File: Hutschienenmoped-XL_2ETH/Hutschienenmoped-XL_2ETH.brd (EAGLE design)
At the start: 166.3 x 101.8 mm, 129 parts, among them J1 638207222005, J13 638207222005, J15 638207222008, J2 645004114822, J4 61300421121, J7 638207222005, J8 638207222007, U4 TLE9250VSJ

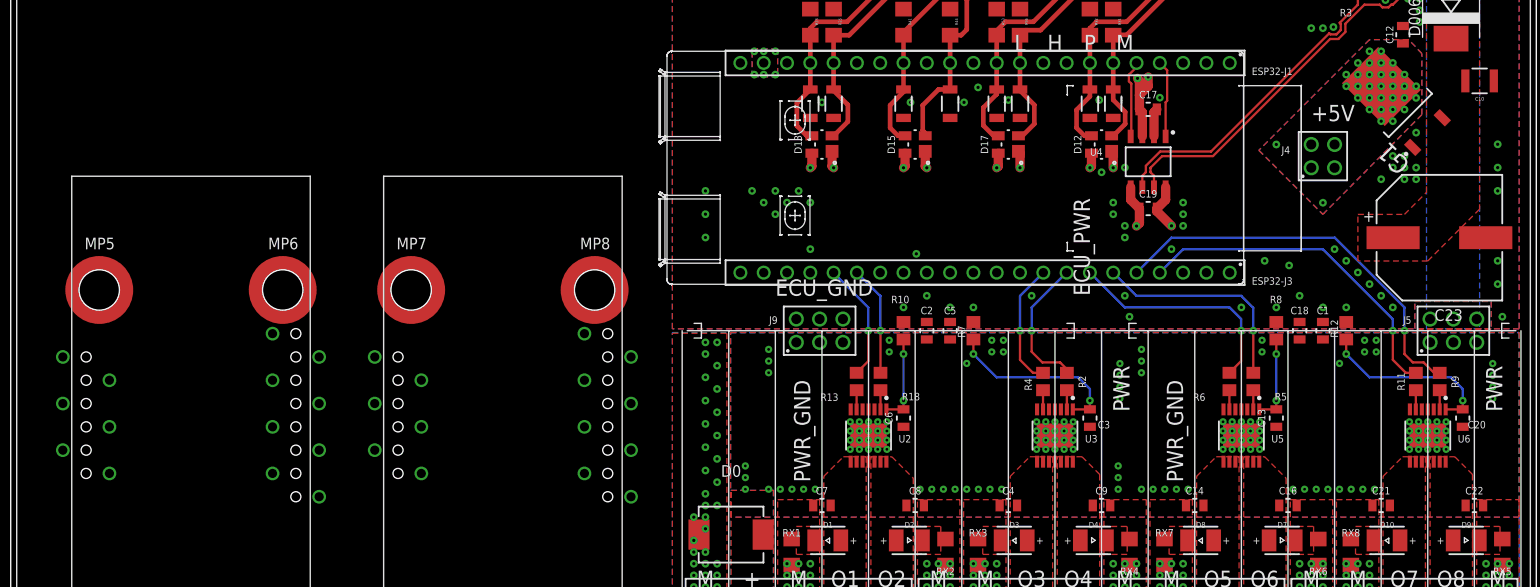
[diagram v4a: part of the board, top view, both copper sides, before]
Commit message: Update grid settings, change font display, adjust pad sizes and hole drills, add new package with 10-pin socket header, modify parameter values for pads and vias. Add symbol for 10-pin socket header THT.
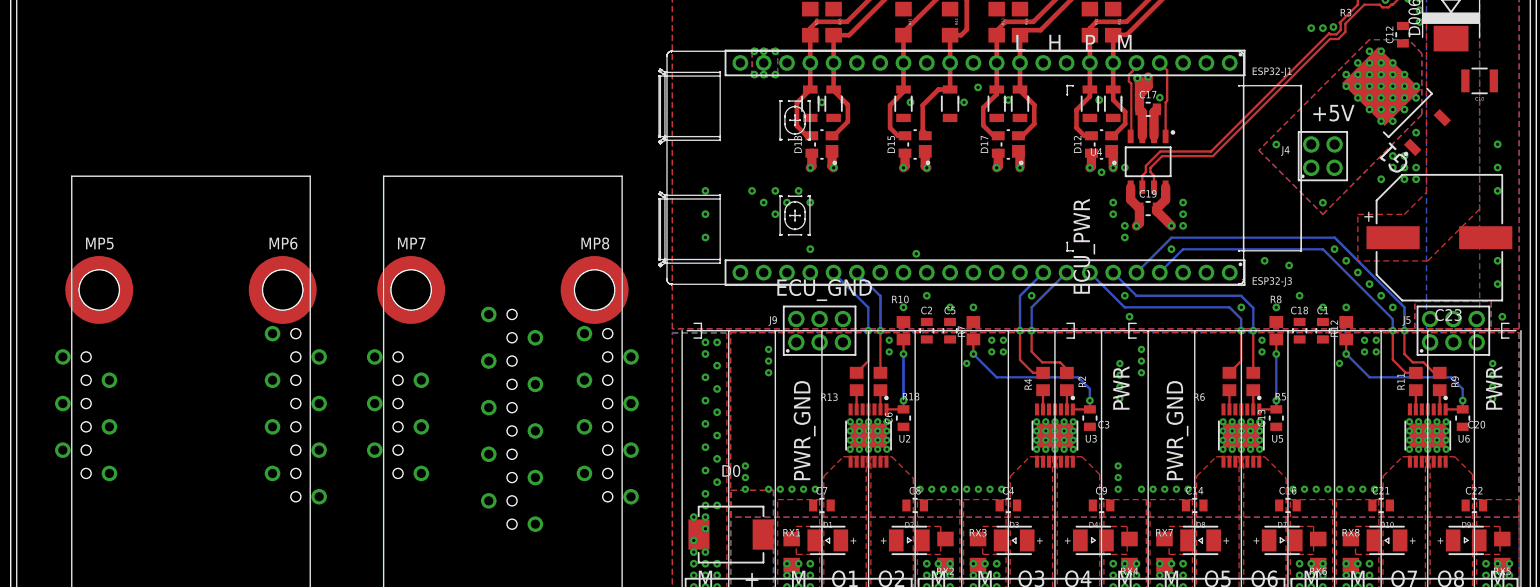
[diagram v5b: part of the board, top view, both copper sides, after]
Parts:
- added J3: 61301015721, Wurth_Connectors_WR-PHD:61301015721
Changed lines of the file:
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@@
 <drawing>
 <settings>
-<setting alwaysvectorfont="no"/>
+<setting alwaysvectorfont="yes"/>
 <setting verticaltext="up"/>
 </settings>
-<grid distance="32.4" unitdist="mm" unit="mm" style="lines" multiple="1" display="yes" altdistance="5" altunitdist="mil" altunit="mil"/>
+<grid distance="1" unitdist="mm" unit="mm" style="lines" multiple="1" display="yes" altdistance="5" altunitdist="mil" altunit="mil"/>
 <layers>
 <layer number="1" name="Top" color="4" fill="1" visible="yes" active="yes"/>
@@
 </layers>
 <board>
-<fusionsync huburn="a.YnVzaW5lc3M6bXNtdWM" projecturn="a.YnVzaW5lc3M6bXNtdWMjMjAyMjAzMTc1MDgxMzE4ODE" f3durn="urn:adsk.wipprod:dm.lineage:ajjTPt2gRBKkWSmyFLQsrw" pcbguid="b123e0b9-a0e3-403d-924e-517ce26273dc" lastpulledtime="2023-10-23T01:33:52Z" lastsyncedchangeguid="" latestrevisionid="f66c36f4-6c79-41b0-bf2f-e42f6f080a47" lastsyncedrevisionid="f66c36f4-6c79-41b0-bf2f-e42f6f080a47" lastboardhashguid="1047857f-715c-b88c-f26d-1f0562ae35e4" lastpushedtime="2024-03-24T11:42:32Z" linktopcb3d="true"/>
+<fusionsync huburn="a.YnVzaW5lc3M6bXNtdWM" projecturn="a.YnVzaW5lc3M6bXNtdWMjMjAyMjAzMTc1MDgxMzE4ODE" f3durn="urn:adsk.wipprod:dm.lineage:ajjTPt2gRBKkWSmyFLQsrw" pcbguid="" lastpulledtime="2023-10-23T01:33:52Z" lastsyncedchangeguid="" latestrevisionid="4beeb25c-c3ea-4695-891d-5bfc398b937a" lastsyncedrevisionid="4beeb25c-c3ea-4695-891d-5bfc398b937a" lastboardhashguid="d47e81b0-323d-8e0b-e760-b965a1c6aebf" lastpushedtime="2024-03-24T11:47:00Z" linktopcb3d="true"/>
 <plain>
 <wire x1="52.04" y1="41.46" x2="50.54" y2="41.46" width="0.1524" layer="22"/>
@@
 <param name="rvMicroViaOuter" value="0"/>
 <param name="rvMicroViaInner" value="0"/>
-<param name="rlMinPadTop" value="0.25mm"/>
+<param name="rlMinPadTop" value="0.35mm"/>
 <param name="rlMaxPadTop" value="0.5mm"/>
 <param name="rlMinPadInner" value="0.15mm"/>
 <param name="rlMaxPadInner" value="0.3mm"/>
-<param name="rlMinPadBottom" value="0.25mm"/>
+<param name="rlMinPadBottom" value="0.35mm"/>
 <param name="rlMaxPadBottom" value="0.5mm"/>
 <param name="rlMinViaOuter" value="0.25mm"/>
@@
 <attribute name="VALUE" x="-7.4622" y="20.1228" size="1.016" layer="28" rot="MR90" align="bottom-right"/>
 </element>
+<element name="J3" library="Wurth_Connectors_WR-PHD" library_urn="urn:adsk.eagle:library:14804658" package="61301015721" package3d_urn="urn:adsk.eagle:package:14805620/2" value=" 61301015721 " x="-16" y="31" smashed="yes" rot="MR270">
+<attribute name="DATASHEET-URL" value="https://www.we-online.com/redexpert/spec/61301015721?ae" x="-16" y="31" size="1.778" layer="28" rot="MR270" display="off"/>
+<attribute name="GENDER" value="Socket Header" x="-16" y="31" size="1.778" layer="28" rot="MR270" display="off"/>
+<attribute name="IR" value="3A" x="-16" y="31" size="1.778" layer="28" rot="MR270" display="off"/>
+<attribute name="MOUNT" value="THT" x="-16" y="31" size="1.778" layer="28" rot="MR270" display="off"/>
+<attribute name="NAME" x="-16.7541" y="44.9272" size="1.016" layer="26" rot="MR270" align="bottom-right"/>
+<attribute name="PACKAGING" value="Tube" x="-16" y="31" size="1.778" layer="28" rot="MR270" display="off"/>
+<attribute name="PART-NUMBER" value=" 61301015721 " x="-16" y="31" size="1.778" layer="28" rot="MR270" display="off"/>
+<attribute name="PINS" value=" 10 " x="-16" y="31" size="1.778" layer="28" rot="MR270" display="off"/>
+<attribute name="PITCH" value="2.54mm" x="-16" y="31" size="1.778" layer="28" rot="MR270" display="off"/>
+<attribute name="ROWS" value="Single" x="-16" y="31" size="1.778" layer="28" rot="MR270" display="off"/>
+<attribute name="TYPE" value="Bottom Entry" x="-16" y="31" size="1.778" layer="28" rot="MR270" display="off"/>
+<attribute name="VALUE" x="-14.1078" y="44.8672" size="1.016" layer="28" rot="MR270" align="bottom-right"/>
+</element>
 </elements>

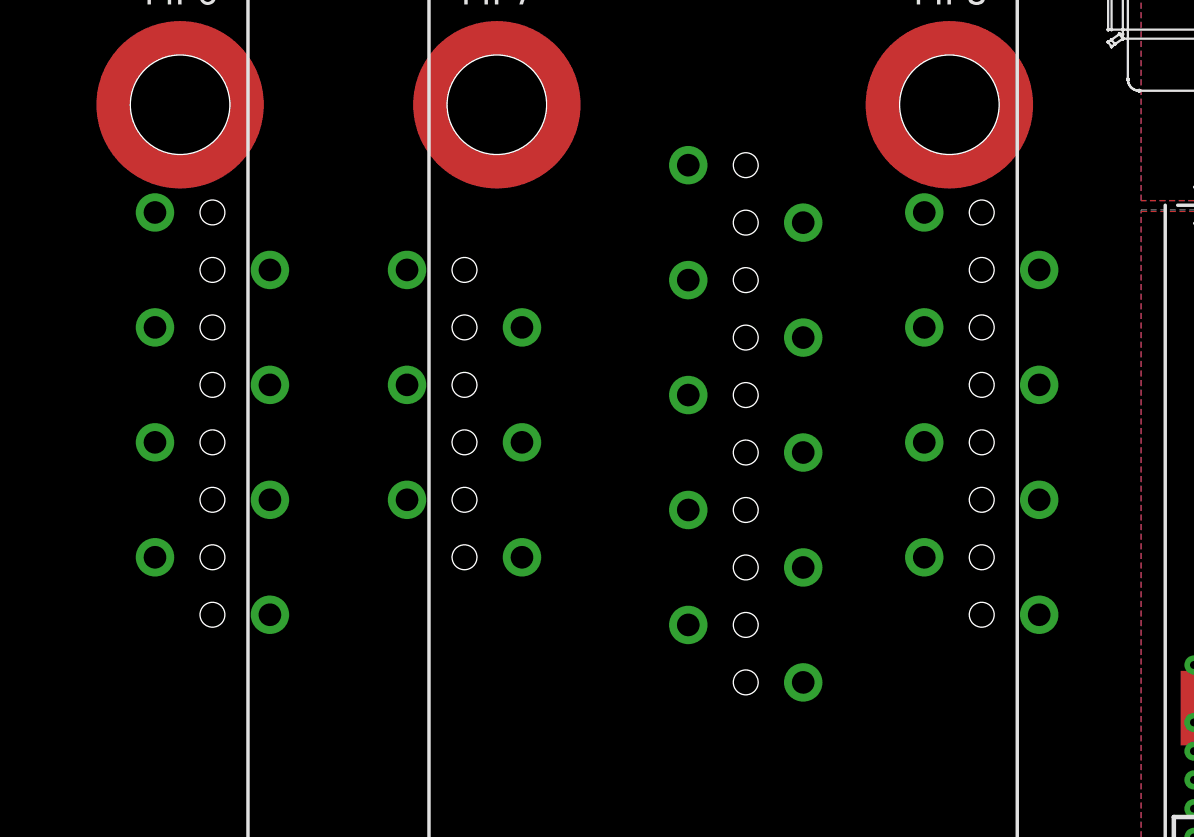
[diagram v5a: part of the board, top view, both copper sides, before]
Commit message: Update layer visibility settings for various elements.
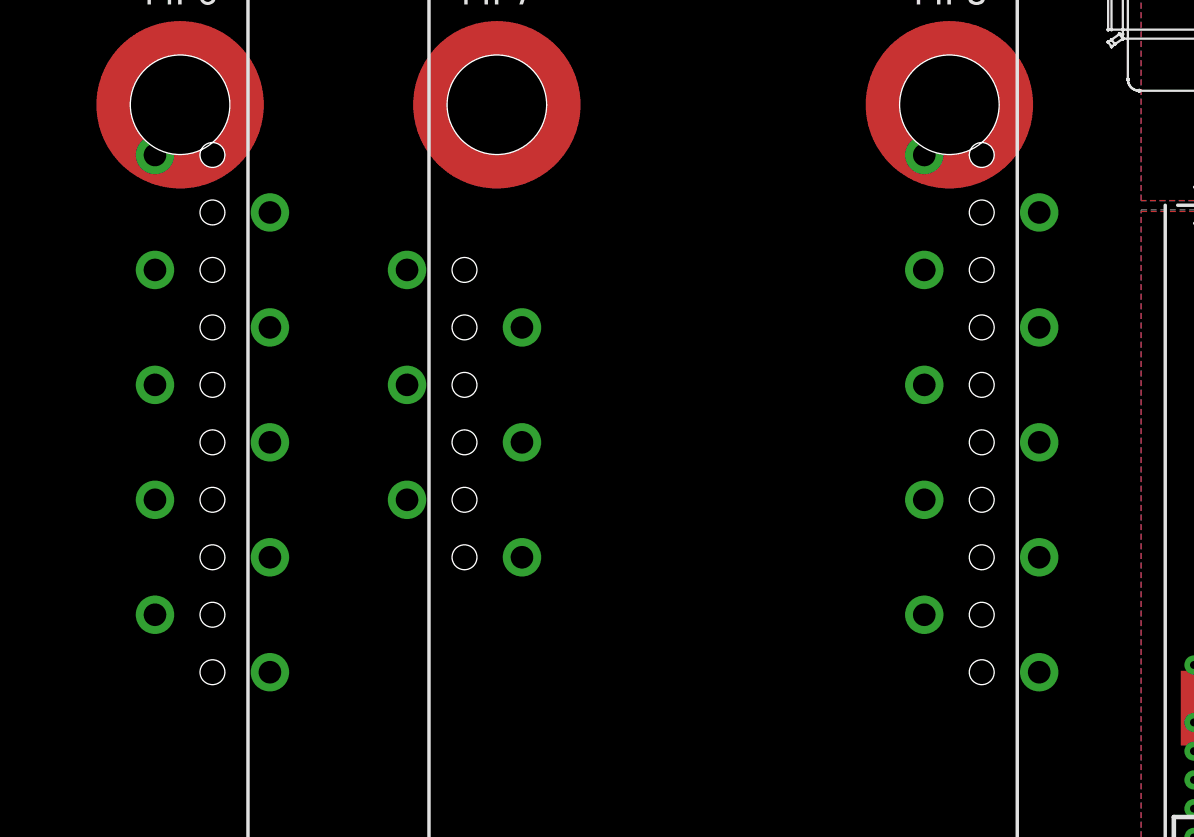
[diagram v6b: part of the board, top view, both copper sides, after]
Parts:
- removed J3: 61301015721, Wurth_Connectors_WR-PHD:61301015721
- W1-J1, W2-J1: value 61300815721 -> 61301015721; device Wurth_Connectors_WR-PHD:61300815721 -> WE-special:61301015721
- turned W1-J1 to 90 degrees

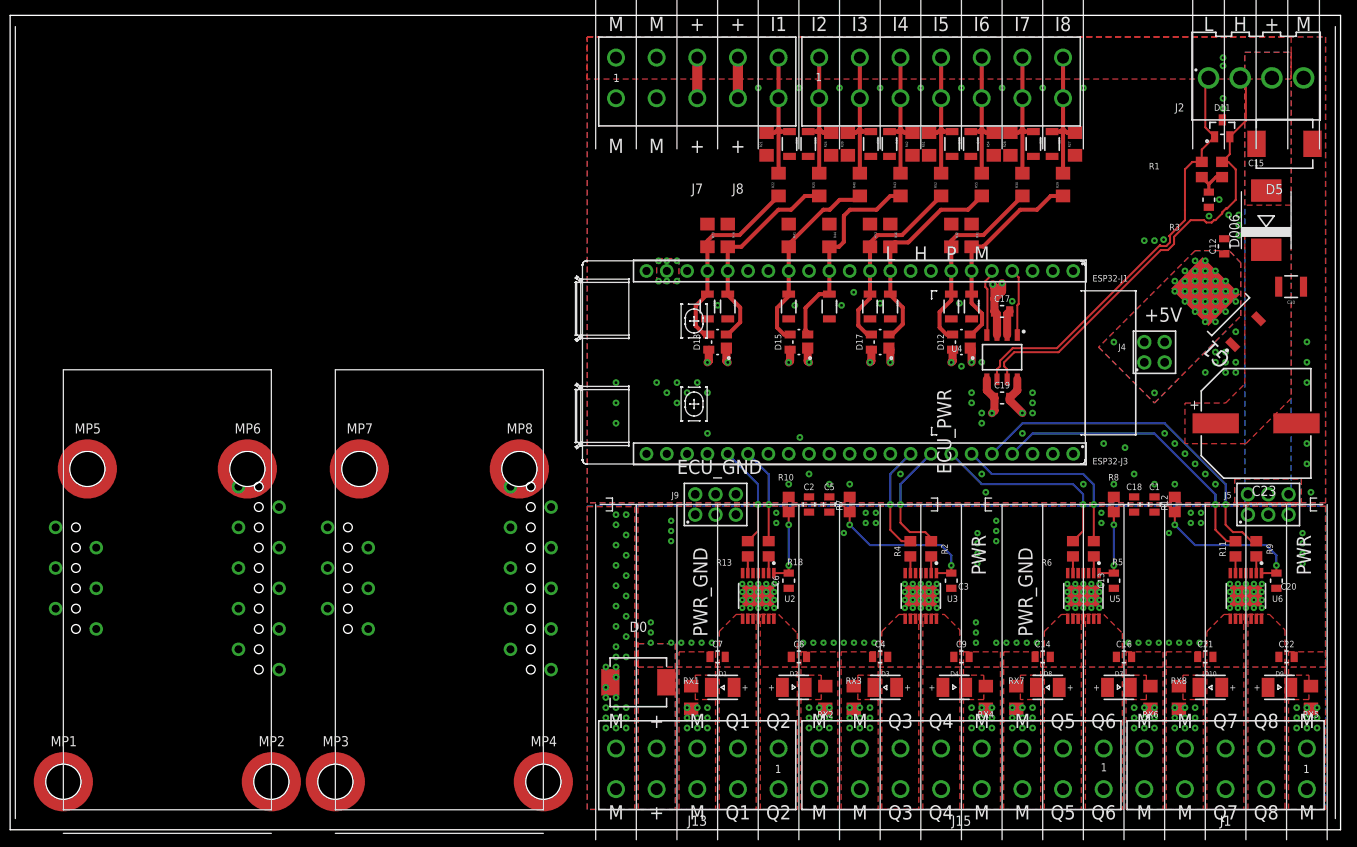
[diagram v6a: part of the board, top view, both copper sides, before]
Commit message: Update package description and pad positions, adjust hole sizes, and modify parameters for better PCB design. Add new contact references, wires, and signals for improved connectivity.
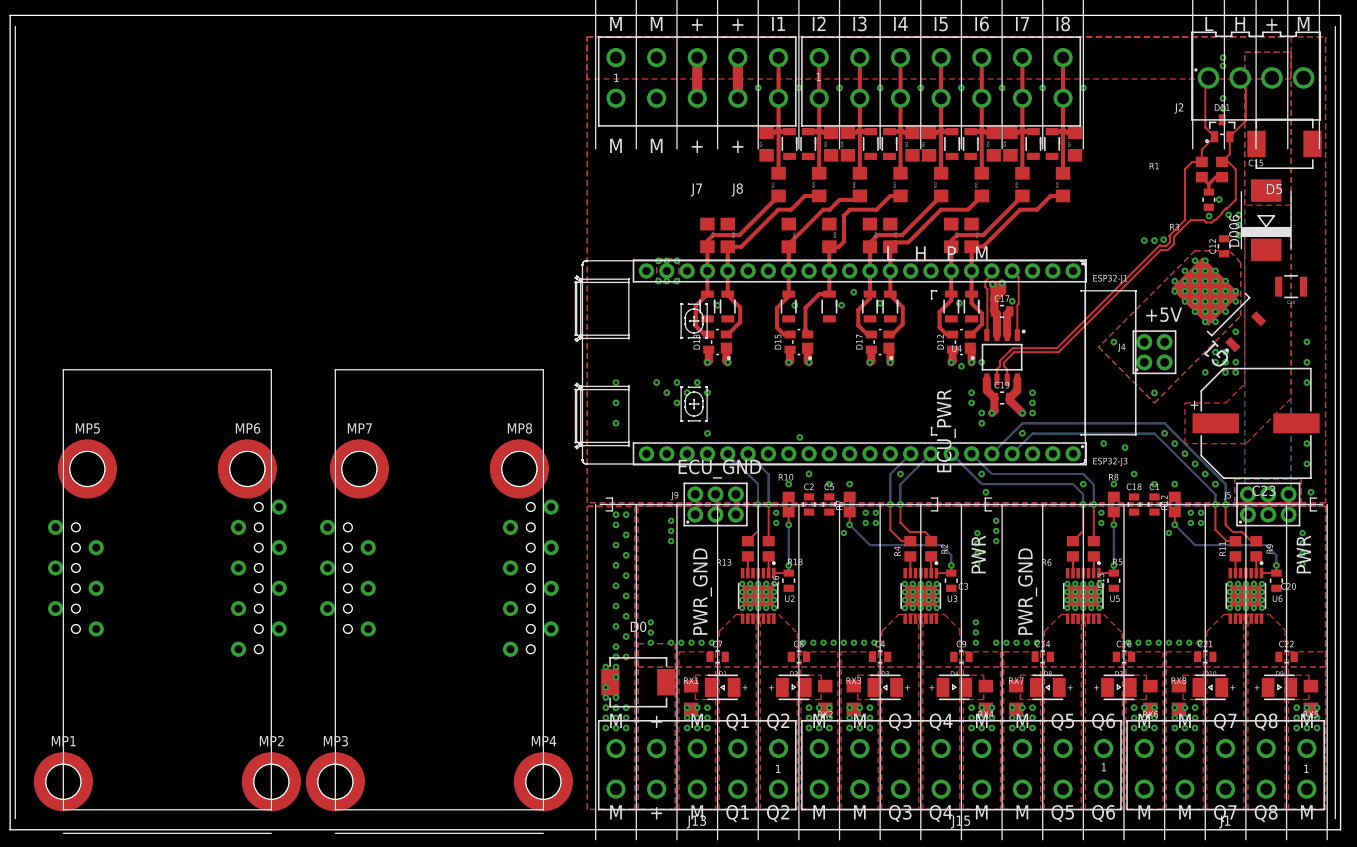
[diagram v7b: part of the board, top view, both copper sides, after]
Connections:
- new net CS0: W1-J1.6
- new net CS1: W2-J1.6
- new net INT0: W1-J2.5
- new net INT1: W2-J2.5
- new net MISO: W1-J1.4, W2-J1.4
- new net MOSI: W1-J1.3, W2-J1.3
- new net RST0: W1-J2.3
- new net RST1: W2-J2.3
- new net SCLK: W1-J1.5, W2-J1.5
- net +3V3: now also W1-J1.7, W1-J1.8, W1-J2.1, W2-J1.7, W2-J1.8, W2-J2.1
- net ECU_GND: now also MP5.1, MP6.1, MP7.1, MP8.1, W1-J1.1, W1-J1.2, W1-J2.6, W2-J1.1, W2-J1.2, W2-J2.6
- net PWR_GND: now also MP1.1, MP2.1, MP3.1, MP4.1
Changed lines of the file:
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@@
 <param name="rvMicroViaOuter" value="0"/>
 <param name="rvMicroViaInner" value="0"/>
-<param name="rlMinPadTop" value="0.35mm"/>
+<param name="rlMinPadTop" value="0.45mm"/>
 <param name="rlMaxPadTop" value="0.5mm"/>
 <param name="rlMinPadInner" value="0.15mm"/>
 <param name="rlMaxPadInner" value="0.3mm"/>
-<param name="rlMinPadBottom" value="0.35mm"/>
+<param name="rlMinPadBottom" value="0.45mm"/>
 <param name="rlMaxPadBottom" value="0.5mm"/>
 <param name="rlMinViaOuter" value="0.25mm"/>
@@
 <contactref element="ESP32-J1" pad="2"/>
 <contactref element="ESP32-J1" pad="1"/>
+<contactref element="W2-J1" pad="8"/>
+<contactref element="W1-J1" pad="8"/>
+<contactref element="W1-J1" pad="7"/>
+<contactref element="W2-J1" pad="7"/>
+<contactref element="W1-J2" pad="1"/>
+<contactref element="W2-J2" pad="1"/>
+<wire x1="-8.11" y1="37.8" x2="-3.03" y2="40.34" width="0" layer="19" extent="1-1"/>
+<wire x1="-25.89" y1="25.1" x2="-8.11" y2="37.8" width="0" layer="19" extent="1-1"/>
+<wire x1="-37.03" y1="40.34" x2="-25.89" y2="25.1" width="0" layer="19" extent="1-1"/>
+<wire x1="-42.11" y1="37.8" x2="-37.03" y2="40.34" width="0" layer="19" extent="1-1"/>
+<wire x1="-59.89" y1="25.1" x2="-42.11" y2="37.8" width="0" layer="19" extent="1-1"/>
+<wire x1="16.51" y1="58.42" x2="-3.03" y2="40.34" width="0" layer="19" extent="1-1"/>
 </signal>
 <signal name="N$17">
@@
 <contactref element="J1" pad="1"/>
 <contactref element="J1" pad="A1"/>
+<contactref element="MP1" pad="1"/>
+<contactref element="MP2" pad="1"/>
+<contactref element="MP3" pad="1"/>
+<contactref element="MP4" pad="1"/>
+<wire x1="-38" y1="6" x2="-64" y2="6" width="0" layer="19" extent="1-1"/>
+<wire x1="-30" y1="6" x2="-38" y2="6" width="0" layer="19" extent="1-1"/>
+<wire x1="-4" y1="6" x2="-30" y2="6" width="0" layer="19" extent="1-1"/>
+<wire x1="3.81" y1="12.72" x2="-4" y2="6" width="0" layer="19" extent="1-1"/>
 </signal>
 <signal name="ECU_GND" class="1">
@@
 <contactref element="ESP32-J3" pad="21"/>
 <contactref element="ESP32-J3" pad="22"/>
+<contactref element="MP5" pad="1"/>
+<contactref element="MP6" pad="1"/>
+<contactref element="MP7" pad="1"/>
+<contactref element="MP8" pad="1"/>
+<contactref element="W1-J1" pad="2"/>
+<contactref element="W1-J1" pad="1"/>
+<contactref element="W2-J1" pad="1"/>
+<contactref element="W2-J1" pad="2"/>
+<contactref element="W2-J2" pad="6"/>
+<contactref element="W1-J2" pad="6"/>
+<wire x1="5.08" y1="50.82" x2="-7" y2="45.1" width="0" layer="19" extent="1-1"/>
+<wire x1="31.75" y1="75.717" x2="36.83" y2="75.717" width="0" layer="19" extent="1-1"/>
+<wire x1="26.67" y1="75.717" x2="31.75" y2="75.717" width="0" layer="19" extent="1-1"/>
+<wire x1="-27" y1="45.1" x2="-7" y2="45.1" width="0" layer="19" extent="1-1"/>
+<wire x1="-30.97" y1="37.8" x2="-27" y2="45.1" width="0" layer="19" extent="1-1"/>
+<wire x1="-41" y1="45.1" x2="-30.97" y2="37.8" width="0" layer="19" extent="1-1"/>
+<wire x1="-37.03" y1="25.1" x2="-30.97" y2="37.8" width="0" layer="19" extent="1-1"/>
+<wire x1="-42.11" y1="22.56" x2="-37.03" y2="25.1" width="0" layer="19" extent="1-1"/>
+<wire x1="-61" y1="45.1" x2="-41" y2="45.1" width="0" layer="19" extent="1-1"/>
+<wire x1="-64.97" y1="37.8" x2="-61" y2="45.1" width="0" layer="19" extent="1-1"/>
+<wire x1="-3.03" y1="25.1" x2="-7" y2="45.1" width="0" layer="19" extent="1-1"/>
+<wire x1="-8.11" y1="22.56" x2="-3.03" y2="25.1" width="0" layer="19" extent="1-1"/>
 </signal>
 <signal name="BOOT">
@@
 <wire x1="5.08" y1="5.08" x2="5.08" y2="10.16" width="0" layer="19" extent="1-1"/>
 </signal>
+<signal name="MOSI">
+<contactref element="W1-J1" pad="3"/>
+<contactref element="W2-J1" pad="3"/>
+<wire x1="-42.11" y1="27.64" x2="-8.11" y2="27.64" width="0" layer="19" extent="1-1"/>
+</signal>
+<signal name="MISO">
+<contactref element="W2-J1" pad="4"/>
+<contactref element="W1-J1" pad="4"/>
+<wire x1="-37.03" y1="30.18" x2="-3.03" y2="30.18" width="0" layer="19" extent="1-1"/>
+</signal>
+<signal name="SCLK">
+<contactref element="W1-J1" pad="5"/>
+<contactref element="W2-J1" pad="5"/>
+<wire x1="-42.11" y1="32.72" x2="-8.11" y2="32.72" width="0" layer="19" extent="1-1"/>
+</signal>
+<signal name="CS0">
+<contactref element="W1-J1" pad="6"/>
+</signal>
+<signal name="CS1">
+<contactref element="W2-J1" pad="6"/>
+</signal>
+<signal name="INT0">
+<contactref element="W1-J2" pad="5"/>
+</signal>
+<signal name="INT1">
+<contactref element="W2-J2" pad="5"/>
+</signal>
+<signal name="RST1">
+<contactref element="W2-J2" pad="3"/>
+</signal>
+<signal name="RST0">
+<contactref element="W1-J2" pad="3"/>
+</signal>
 </signals>
